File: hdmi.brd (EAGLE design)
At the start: 160 x 100 mm, 130 parts, among them U0 6SLX45CSG324, U1 MT41J64M16, U2 TPD12S016RKTR, U3 TPD12S016RKTR, U4 TPD12S016RKTR, U5 MNR18, U6 MNR18

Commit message: +prj-hdmi.lbr, +5V protection
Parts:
- removed R43: 4.7k, resistor:R0402
- removed U$12: PJ-037A, con-cui:PJ-037A
- removed U$13: FERRITE0603, inductors:0603
- added C15: 0.47n, rcl:C0402
- added R46: 1k, resistor:R0402
- added U$15: PJ-037A, prj-hdmi:PJ-037A
- added U$16: FERRITE0603, inductors:0603
- added U$17: TPS2592BA, prj-hdmi:DRC-S-PVSON-N10
- CONN0, CONN1, CONN2: device con-fci:HDMI_TYPE_A_RECEPTICAL -> prj-hdmi:HDMI_TYPE_A_RECEPTICAL
- CONN3: device con-usb-3:USB-MB-S -> prj-hdmi:USB-MB-S
- IC1: device ftdichip-3:QFN64 -> prj-hdmi:QFN64
- R42: value 10k -> 100k
- U$1: device Abracon:ABM8G-32X25 -> prj-hdmi:ABM8G-32X25
- U$5: device Microchip_By_element14_Batch_1:SOT95P280X145-6N -> prj-hdmi:SOT95P280X145-6N
- U$6: device Micrel Inc:QFN-26-4X4 -> prj-hdmi:QFN-26-4X4
- U$9: device memory-micron:V-PDFN-8_8X6 -> prj-hdmi:V-PDFN-8_8X6
- U0: device xilinx_devices_V6:CS324 -> prj-hdmi:CS324
- U1: device memory-micron:FBGA96-JT -> prj-hdmi:FBGA96-JT
- U2, U3, U4: device Texas Instruments:UQFN24 -> prj-hdmi:UQFN24
- moved R42 97.8 mm to (-148.6, -733.9)
- moved U0 0.31 mm to (-39.4, 9.20)
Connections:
- net N$49 renamed USB_5V_DISABLE
- removed net USB_5V_ERR: R45.1, U$10.4
- new net N$32: C15.1, U$17.1
- new net N$36: R42.2, U$17.10
- new net USB_5V_ACK#: R45.1, R46.1, U$10.4
- new net USB_5V_OFF: R46.2
- net +3V3: now also R26.1
- net +5V: now also U$17.6, U$17.7, U$17.8; no longer R43.2
- net CENTER: now also U$15.CENTER, U$16.1; no longer U$12.CENTER, U$13.1
- net GND: now also C15.2, U$15.BARREL, U$17.TH, U$17.TH@1, U$17.TH@2; no longer U$12.BARREL
- net N$29: now also U$16.2, U$17.2, U$17.3, U$17.4, U$17.5; no longer R26.1
- net USB_PWRSAVE#: no longer R42.2, R43.1

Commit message: began mergin and cleaning up libraries
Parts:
- removed C7: 100u, rcl:C1206
- removed U$11: FERRITE0603, inductors:0603
- added L6: 1A, prj-hdmi:0603
- added R43: 10k, resistor:R0402
- L1, L2, L3: value CIG22E -> 1u; device inductors:2520 -> prj-hdmi:1008
- L4, L5: value FERRITE0402 -> 1A; device inductors:0402 -> prj-hdmi:0402
- LED1, LED2: device led:CHIP-LED0603 -> prj-hdmi:LED-0603
- R42: value 100k -> 47k
- U$10: value TPD4S014DSQRSON -> TPD4S014SON
- U$16: value FERRITE0603 -> 4A; device inductors:0603 -> prj-hdmi:0603
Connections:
- net +1V5: no longer C7.1
- net +3V3: now also R43.2; no longer LED2.A
- net GND: no longer C7.2
- net N$45: now also L6.1; no longer U$11.1
- net N$48: now also L6.2; no longer U$11.2
- net USB_PWRSAVE#: now also R43.1
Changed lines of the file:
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@@
 <element name="C5" library="rcl" package="C0402" value="4.7u" x="-55.88" y="-52.07"/>
 <element name="C6" library="rcl" package="C0402" value="0.47u" x="-55.88" y="-57.15"/>
-<element name="C7" library="rcl" package="C1206" value="100u" x="-54.61" y="-63.5"/>
 <element name="C8" library="rcl" package="C0402" value="0.47u" x="-55.88" y="-69.85"/>
 <element name="R7" library="resistor" package="R0402" value="120" x="-55.88" y="-74.93"/>
@@
 <element name="C48" library="rcl" package="C0402" value="4.7u" x="-113.03" y="-405.13"/>
 <element name="C49" library="rcl" package="C1206" value="100u" x="-111.76" y="-411.48"/>
-<element name="L1" library="inductors" package="2520" value="CIG22E" x="-118.11" y="-411.48"/>
-<element name="L2" library="inductors" package="2520" value="CIG22E" x="-123.19" y="-411.48"/>
-<element name="L3" library="inductors" package="2520" value="CIG22E" x="-128.27" y="-411.48"/>
+<element name="L1" library="prj-hdmi" package="1008" value="1u" x="-118.11" y="-411.48"/>
+<element name="L2" library="prj-hdmi" package="1008" value="1u" x="-123.19" y="-411.48"/>
+<element name="L3" library="prj-hdmi" package="1008" value="1u" x="-128.27" y="-411.48"/>
 <element name="R15" library="resistor" package="R0402" value="309k" x="-128.27" y="-417.83"/>
 <element name="R16" library="resistor" package="R0402" value="71.5k" x="-128.27" y="-422.91"/>
@@
 <element name="R25" library="resistor" package="R0402" value="10k" x="-128.27" y="-483.87"/>
 <element name="R26" library="resistor" package="R0402" value="10k" x="-128.27" y="-488.95"/>
-<element name="L4" library="inductors" package="0402" value="FERRITE0402" x="-128.27" y="-494.03"/>
-<element name="L5" library="inductors" package="0402" value="FERRITE0402" x="-128.27" y="-499.11"/>
+<element name="L4" library="prj-hdmi" package="0402" value="1A" x="-128.27" y="-494.03"/>
+<element name="L5" library="prj-hdmi" package="0402" value="1A" x="-128.27" y="-499.11"/>
 <element name="C53" library="resistor" package="C0402" value="0.1u" x="-128.27" y="-504.19"/>
 <element name="C54" library="resistor" package="C0402" value="4.7u" x="-128.27" y="-509.27"/>
@@
 <element name="R32" library="resistor" package="R0402" value="1k" x="-128.27" y="-574.04"/>
 <element name="R33" library="resistor" package="R0402" value="1k" x="-128.27" y="-579.12"/>
-<element name="LED1" library="led" package="CHIP-LED0603" value="Yellow" x="-133.35" y="-580.39"/>
+<element name="LED1" library="prj-hdmi" package="LED-0603" value="Yellow" x="-133.35" y="-580.39"/>
 <element name="R34" library="resistor" package="R0402" value="4.7k" x="-133.35" y="-584.2"/>
 <element name="R35" library="resistor" package="R0402" value="10k" x="-133.35" y="-589.28"/>
@@
 <element name="R40" library="resistor" package="R0402" value="100" x="-143.51" y="-619.76"/>
 <element name="R41" library="resistor" package="R0402" value="1k" x="-143.51" y="-631.19"/>
-<element name="LED2" library="led" package="CHIP-LED0603" value="Green" x="-142.24" y="-627.38"/>
-<element name="U$11" library="inductors" package="0603" value="FERRITE0603" x="-143.51" y="-650.24"/>
-<element name="U$10" library="Texas Instruments" package="SON10" value="TPD4S014DSQRSON" x="-148.59" y="-654.05"/>
+<element name="LED2" library="prj-hdmi" package="LED-0603" value="Green" x="-142.24" y="-627.38"/>
+<element name="L6" library="prj-hdmi" package="0603" value="1A" x="-143.51" y="-650.24"/>
+<element name="U$10" library="Texas Instruments" package="SON10" value="TPD4S014SON" x="-148.59" y="-654.05"/>
 <element name="R44" library="resistor" package="R0402" value="10k" x="-148.59" y="-660.4"/>
 <element name="R45" library="resistor" package="R0402" value="10k" x="-148.59" y="-680.72"/>
 <element name="R46" library="resistor" package="R0402" value="1k" x="-148.59" y="-690.6768"/>
 <element name="U$15" library="prj-hdmi" package="PJ-037A" value="PJ-037A" x="-141.8844" y="-707.5424"/>
-<element name="U$16" library="inductors" package="0603" value="FERRITE0603" x="-148.59" y="-724.3064"/>
+<element name="U$16" library="prj-hdmi" package="0603" value="4A" x="-148.59" y="-724.3064"/>
 <element name="U$17" library="prj-hdmi" package="DRC-S-PVSON-N10" value="TPS2592BA" x="-147.066" y="-717.9564"/>
 <element name="C15" library="rcl" package="C0402" value="0.47n" x="-148.59" y="-729.0562"/>
-<element name="R42" library="resistor" package="R0402" value="100k" x="-148.59" y="-733.933"/>
+<element name="R42" library="resistor" package="R0402" value="47k" x="-148.59" y="-733.933"/>
+<element name="R43" library="resistor" package="R0402" value="10k" x="-148.59" y="-738.9368"/>
 </elements>
 <signals>
@@
 <contactref element="C6" pad="2"/>
 <contactref element="C5" pad="2"/>
-<contactref element="C7" pad="2"/>
 <contactref element="C13" pad="2"/>
 <contactref element="C16" pad="2"/>
@@
 <wire x1="-55.23" y1="-74.93" x2="-55.23" y2="-80.01" width="0" layer="19" extent="1-1"/>
 <wire x1="-55.23" y1="-69.85" x2="-55.23" y2="-74.93" width="0" layer="19" extent="1-1"/>
-<wire x1="-53.21" y1="-63.5" x2="-55.23" y2="-69.85" width="0" layer="19" extent="1-1"/>
-<wire x1="-55.23" y1="-57.15" x2="-53.21" y2="-63.5" width="0" layer="19" extent="1-1"/>
+<wire x1="-55.23" y1="-57.15" x2="-55.23" y2="-69.85" width="0" layer="19" extent="1-1"/>
 <wire x1="-55.23" y1="-52.07" x2="-55.23" y2="-57.15" width="0" layer="19" extent="1-1"/>
 <wire x1="-56.53" y1="-41.91" x2="-55.23" y2="-52.07" width="0" layer="19" extent="1-1"/>
@@
 <contactref element="R38" pad="2"/>
 <contactref element="R39" pad="2"/>
-<contactref element="LED2" pad="A"/>
 <contactref element="R45" pad="2"/>
 <contactref element="R26" pad="1"/>
+<contactref element="R43" pad="2"/>
 <wire x1="-142.86" y1="-609.6" x2="-142.86" y2="-614.68" width="0" layer="19" extent="1-1"/>
 <wire x1="-142.86" y1="-604.52" x2="-142.86" y2="-609.6" width="0" layer="19" extent="1-1"/>
@@
 <wire x1="-132.7" y1="-584.2" x2="-136.92" y2="-589.91" width="0" layer="19" extent="1-1"/>
 <wire x1="-133.35" y1="-581.14" x2="-132.7" y2="-584.2" width="0" layer="19" extent="1-1"/>
-<wire x1="-142.24" y1="-628.13" x2="-142.86" y2="-614.68" width="0" layer="19" extent="1-1"/>
 <wire x1="-127.62" y1="-553.72" x2="-133.35" y2="-581.14" width="0" layer="19" extent="1-1"/>
 <wire x1="-128.92" y1="-534.67" x2="-127.62" y2="-553.72" width="0" layer="19" extent="1-1"/>
@@
 <wire x1="-89.55" y1="-227.33" x2="-90.245" y2="-266.68" width="0" layer="19" extent="1-1"/>
 <wire x1="-90.245" y1="-205.72" x2="-89.55" y2="-227.33" width="0" layer="19" extent="1-1"/>
-<wire x1="-147.94" y1="-680.72" x2="-142.24" y2="-628.13" width="0" layer="19" extent="1-1"/>
+<wire x1="-147.94" y1="-680.72" x2="-142.86" y2="-614.68" width="0" layer="19" extent="1-1"/>
+<wire x1="-147.94" y1="-738.9368" x2="-147.94" y2="-680.72" width="0" layer="19" extent="1-1"/>
 <wire x1="-43" y1="5.6" x2="-90.245" y2="-205.72" width="0" layer="19" extent="1-1"/>
 <wire x1="-41.4" y1="8.8" x2="-43" y2="5.6" width="0" layer="19" extent="1-1"/>
@@
 <contactref element="C1" pad="1"/>
 <contactref element="C8" pad="1"/>
-<contactref element="C7" pad="1"/>
 <contactref element="C5" pad="1"/>
 <contactref element="C6" pad="1"/>
@@
 <wire x1="-56.53" y1="-80.01" x2="-56.53" y2="-85.09" width="0" layer="19" extent="1-1"/>
 <wire x1="-56.53" y1="-69.85" x2="-56.53" y2="-80.01" width="0" layer="19" extent="1-1"/>
-<wire x1="-56.01" y1="-63.5" x2="-56.53" y2="-69.85" width="0" layer="19" extent="1-1"/>
-<wire x1="-56.53" y1="-57.15" x2="-56.01" y2="-63.5" width="0" layer="19" extent="1-1"/>
+<wire x1="-56.53" y1="-57.15" x2="-56.53" y2="-69.85" width="0" layer="19" extent="1-1"/>
 <wire x1="-56.53" y1="-52.07" x2="-56.53" y2="-57.15" width="0" layer="19" extent="1-1"/>
 <wire x1="-56.53" y1="-22.86" x2="-56.53" y2="-52.07" width="0" layer="19" extent="1-1"/>
@@
 <signal name="USB_PWRSAVE#">
 <contactref element="IC1" pad="59"/>
+<contactref element="R43" pad="1"/>
+<wire x1="-149.24" y1="-738.9368" x2="-83.8" y2="-321.99" width="0" layer="19" extent="1-1"/>
 </signal>
 <signal name="N$45" class="1">
 <contactref element="CONN3" pad="VBUS"/>
-<contactref element="U$11" pad="1"/>
+<contactref element="L6" pad="1"/>
 <wire x1="-144.36" y1="-650.24" x2="-95.29" y2="-328.6" width="0" layer="19" extent="1-1"/>
 </signal>
@@
 </signal>
 <signal name="N$48">
-<contactref element="U$11" pad="2"/>
+<contactref element="L6" pad="2"/>
 <contactref element="U$10" pad="9"/>
 <contactref element="U$10" pad="10"/>

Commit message: +5V supply zener diode and minor misc. changes
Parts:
- removed C49: 100u, rcl:C1206
- added C19: 0.1u, prj-hdmi:0603
- added C7: 100u, prj-hdmi:0603
- added R47: 50, resistor:R0402
- added R48: 100, resistor:R0402
- added U$11: 20V, prj-hdmi:SOD123FL
- L1, L2, L3: value 1u -> 1u, 2.3A
- U$16: value 4A -> 3A
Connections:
- net +3V3: now also R27.2; no longer LED1.A
- net +5V: now also R41.2; no longer C49.1
- net CENTER: now also U$11.C
- net GND: now also C19.2, C7.2, LED2.C, R48.1, U$11.A, U$6.11, U$6.24, U$6.SGND; no longer C49.2, R41.1
- net N$29: now also C19.1, R47.2; no longer U$17.2
- net N$30: now also R47.1, R48.2, U$17.2; no longer U$6.11, U$6.24, U$6.SGND
- net N$33: now also LED1.C; no longer R27.1
- net N$38: now also LED1.A, R27.1; no longer LED1.C, R27.2
- net N$47: now also LED2.A, R41.1; no longer LED2.C, R41.2
- net N$48: now also C7.1

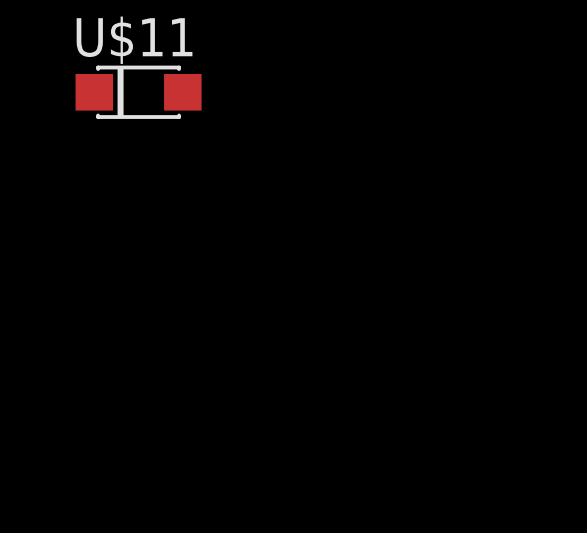
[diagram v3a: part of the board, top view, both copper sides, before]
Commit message: +N-MOSFET at 5V supply, HDMI connector pin swap, minor wiring changes
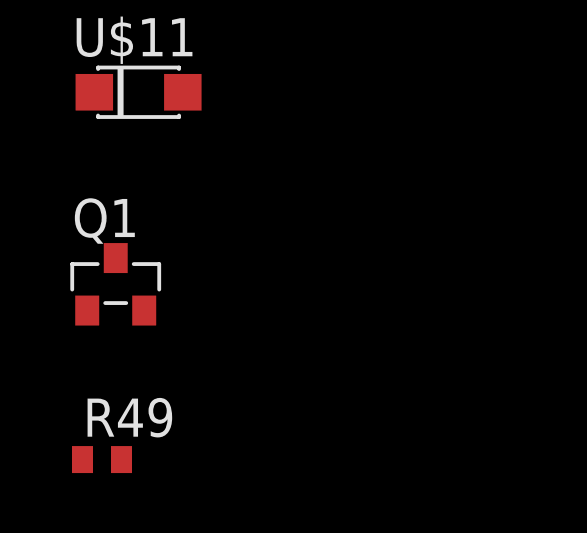
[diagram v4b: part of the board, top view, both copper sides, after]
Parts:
- added Q1: N-MOSFETSOT23, prj-hdmi:SOT23
- added R49: 1k, resistor:R0402
- CONN3: value (none) -> USBMB-S
- IC1: value (none) -> FT2232HQ
- R47: value 50 -> 1k
- R48: value 100 -> 4.7k
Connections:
- removed net 3V3: C13.1, C14.1, C16.1, C17.1, C18.1, C20.1, C21.1, C22.1, C24.1, R29.2, U0.B10, U0.B15, U0.B5, U0.D13, U0.D7, U0.E10, U0.E17, U0.G15, U0.J14, U0.J17, U0.M15, U0.P9, U0.R12, U0.R17, U0.R6, U0.T15, U0.U14, U0.U4, U0.U9
- removed net 3V4: C25.1, C26.1, C27.1, C28.1, C33.1
- removed net 3V5: C29.1, C30.1, C31.1, C32.1
- removed net N$19: C52.2, R20.2
- removed net N$2: IC1.3, U$1.1
- removed net N$4: C44.2, U$1.4
- new net N$49: Q1.1, U$17.9
- new net OUT@8: Q1.2, R49.2, U$17.6, U$17.7, U$17.8
- net +1V2: now also C29.1, C30.1, C31.1, C32.1
- net +3V3: now also C13.1, C14.1, C16.1, C17.1, C18.1, C20.1, C21.1, C22.1, C24.1, C25.1, C26.1, C27.1, C28.1, C33.1, C57.2, R29.2, U0.B10, U0.B15, U0.B5, U0.D13, U0.D7, U0.E10, U0.E17, U0.G15, U0.J14, U0.J17, U0.M15, U0.P9, U0.R12, U0.R17, U0.R6, U0.T15, U0.U14, U0.U4, U0.U9; no longer C57.1
- net +5V: now also Q1.3; no longer U$17.6, U$17.7, U$17.8
- net DDR3_A12: now also U0.G6
- net DDR3_DQ3: now also U1.F8
- net DDR3_DQ4: no longer U1.F8
- net GND: now also C43.2, C44.2, C52.2, C57.1, R20.2, U$1.2, U$1.4; no longer C43.1, C44.1, C57.2
- net HDMI_RX0_CEC: now also U2.6; no longer U2.24
- net HDMI_RX0_CEC_3V3: now also U2.24; no longer U2.6
- net HDMI_RX0_SCL_3V3: now also U2.1; no longer U2.7
- net HDMI_RX0_SCL_5V: now also U2.7; no longer U2.1
- net HDMI_RX0_SDA_3V3: now also U2.2; no longer U2.8
- net HDMI_RX0_SDA_5V: now also U2.8; no longer U2.2
- net HDMI_RX1_CEC: now also U3.6; no longer U3.24
- net HDMI_RX1_CEC_3V3: now also U3.24; no longer U3.6
- net HDMI_RX1_SCL_3V3: now also U3.1; no longer U3.7
- net HDMI_RX1_SCL_5V: now also U3.7; no longer U3.1
- net HDMI_RX1_SDA_3V3: now also U3.2; no longer U3.8
- net HDMI_RX1_SDA_5V: now also U3.8; no longer U3.2
- net HDMI_TX0_CEC: now also U4.6; no longer U4.24
- net HDMI_TX0_CEC_3V3: now also U4.24; no longer U4.6
- net HDMI_TX0_HPD_3V3: now also U4.3; no longer U4.9
- net HDMI_TX0_HPD_5V: now also U4.9; no longer U4.3
- net HDMI_TX0_SCL_3V3: now also U4.1; no longer U4.7
- net HDMI_TX0_SCL_5V: now also U4.7; no longer U4.1
- net HDMI_TX0_SDA_3V3: now also U4.2; no longer U4.8
- net HDMI_TX0_SDA_5V: now also U4.8; no longer U4.2
- net N$1: now also C44.1
- net N$10: now also U$5.3
- net N$5: now also C43.1, IC1.3, U$1.1; no longer C43.2, U$1.2
- net USB_5V_DISABLE: now also R49.1

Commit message: +Oscillator
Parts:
- added C23: 0.1u, rcl:C0402
- added U7: 20Mhz, prj-hdmi:CRYSTAL-OSC-SMD-2.5X2
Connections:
- new net FPGA_OSC: U0.T10, U7.3
- net +3V3: now also C23.1, U7.1, U7.4
- net GND: now also C23.2, U7.2
- net HDMI_TX0_CEC_3V3: now also U0.N8; no longer U0.T10
- net HDMI_TX0_HPD_3V3: now also U0.M8; no longer U0.R10
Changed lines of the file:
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@@
 <element name="Q1" library="prj-hdmi" package="SOT23" value="N-MOSFETSOT23" x="-148.1328" y="-773.4554"/>
 <element name="R49" library="resistor" package="R0402" value="1k" x="-148.59" y="-779.272"/>
+<element name="U7" library="prj-hdmi" package="CRYSTAL-OSC-SMD-2.5X2" value="20Mhz" x="-151.9174" y="-778.764"/>
+<element name="C23" library="rcl" package="C0402" value="0.1u" x="-153.4668" y="-784.1488"/>
 </elements>
 <signals>
@@
 <contactref element="U$1" pad="4"/>
 <contactref element="C57" pad="1"/>
+<contactref element="C43" pad="2"/>
+<contactref element="C44" pad="2"/>
 <contactref element="U$1" pad="2"/>
-<contactref element="C44" pad="2"/>
-<contactref element="C43" pad="2"/>
+<contactref element="U7" pad="2"/>
+<contactref element="C23" pad="2"/>
 <wire x1="-88.25" y1="-161.29" x2="-88.25" y2="-166.37" width="0" layer="19" extent="1-1"/>
 <wire x1="-88.25" y1="-171.45" x2="-88.25" y2="-166.37" width="0" layer="19" extent="1-1"/>
@@
 <wire x1="-149.24" y1="-761.5936" x2="-147.74" y2="-753.5672" width="0" layer="19" extent="1-1"/>
 <wire x1="-145.8958" y1="-767.0292" x2="-149.24" y2="-761.5936" width="0" layer="19" extent="1-1"/>
+<wire x1="-151.0174" y1="-779.464" x2="-145.8958" y2="-767.0292" width="0" layer="19" extent="1-1"/>
+<wire x1="-152.8168" y1="-784.1488" x2="-151.0174" y2="-779.464" width="0" layer="19" extent="1-1"/>
 </signal>
 <signal name="+3V3" class="1">
@@
 <contactref element="C33" pad="1"/>
 <contactref element="C57" pad="2"/>
+<contactref element="U7" pad="1"/>
+<contactref element="U7" pad="4"/>
+<contactref element="C23" pad="1"/>
 <wire x1="-142.86" y1="-609.6" x2="-142.86" y2="-614.68" width="0" layer="19" extent="1-1"/>
 <wire x1="-142.86" y1="-604.52" x2="-142.86" y2="-609.6" width="0" layer="19" extent="1-1"/>
@@
 <wire x1="-147.94" y1="-680.72" x2="-142.86" y2="-614.68" width="0" layer="19" extent="1-1"/>
 <wire x1="-147.94" y1="-738.9368" x2="-147.94" y2="-680.72" width="0" layer="19" extent="1-1"/>
+<wire x1="-152.8174" y1="-778.064" x2="-147.94" y2="-738.9368" width="0" layer="19" extent="1-1"/>
+<wire x1="-152.8174" y1="-779.464" x2="-152.8174" y2="-778.064" width="0" layer="19" extent="1-1"/>
+<wire x1="-154.1168" y1="-784.1488" x2="-152.8174" y2="-779.464" width="0" layer="19" extent="1-1"/>
 <wire x1="-43.8" y1="3.2" x2="-56.53" y2="-107.95" width="0" layer="19" extent="1-1"/>
 <wire x1="-42.2" y1="4.8" x2="-43.8" y2="3.2" width="0" layer="19" extent="1-1"/>
@@
 <signal name="HDMI_TX0_HPD_3V3">
 <contactref element="U4" pad="3"/>
-<contactref element="U0" pad="R10"/>
-<wire x1="-39" y1="4.8" x2="-89.27" y2="-303.415" width="0" layer="19" extent="1-1"/>
+<contactref element="U0" pad="M8"/>
+<wire x1="-40.6" y1="7.2" x2="-89.27" y2="-303.415" width="0" layer="19" extent="1-1"/>
 </signal>
 <signal name="HDMI_TX0_CEC_3V3">
 <contactref element="U4" pad="24"/>
-<contactref element="U0" pad="T10"/>
-<wire x1="-39" y1="4" x2="-90.245" y2="-302.64" width="0" layer="19" extent="1-1"/>
+<contactref element="U0" pad="N8"/>
+<wire x1="-40.6" y1="6.4" x2="-90.245" y2="-302.64" width="0" layer="19" extent="1-1"/>
 </signal>
 <signal name="HDMI_TX0_SCL_3V3">
@@
 <wire x1="-86.95" y1="-323.64" x2="-109.05" y2="-333.54" width="0" layer="19" extent="1-1"/>
 </signal>
+<signal name="FPGA_OSC">
+<contactref element="U0" pad="T10"/>
+<contactref element="U7" pad="3"/>
+<wire x1="-39" y1="4" x2="-151.0174" y2="-778.064" width="0" layer="19" extent="1-1"/>
+</signal>
 </signals>

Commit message: +IO
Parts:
- removed C23: 0.1u, rcl:C0402
- removed U7: 20Mhz, prj-hdmi:CRYSTAL-OSC-SMD-2.5X2
- added C49: 0.1u, rcl:C0402
- added SV1: JTAG, prj-hdmi:MA06-1
- added SV2: FE10-2, prj-hdmi:FE10-2
- added U$12: SN74LVC8T245RHLR, prj-hdmi:RHL_R-PVQFN-N24
- added U8: 20Mhz, prj-hdmi:CRYSTAL-OSC-SMD-2.5X2
- L1, L2, L3: value 1u, 2.3A -> 1u, 3A
- R44: value 10k -> 4.7k
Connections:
- removed net FPGA_OSC: U0.T10, U7.3
- removed net USB_PWREN#: IC1.60
- new net FPGA_OSC1: U0.A9, U8.3
- new net IO_0: SV2.5, U0.B11
- new net IO_1: SV2.7, U0.A11
- new net IO_10: U$12.5, U0.C15
- new net IO_10_5V: SV2.10, U$12.19
- new net IO_11: U$12.6, U0.A15
- new net IO_11_5V: SV2.12, U$12.18
- new net IO_12: U$12.7, U0.D14
- new net IO_12_5V: SV2.14, U$12.17
- new net IO_13: U$12.8, U0.C14
- new net IO_13_5V: SV2.16, U$12.16
- new net IO_14: U$12.9, U0.B16
- new net IO_14_5V: SV2.18, U$12.15
- new net IO_15: U$12.10, U0.A16
- new net IO_15_5V: SV2.20, U$12.14
- new net IO_2: SV2.9, U0.B12
- new net IO_3: SV2.11, U0.A12
- new net IO_4: SV2.13, U0.C13
- new net IO_5: SV2.15, U0.A13
- new net IO_6: SV2.17, U0.B14
- new net IO_7: SV2.19, U0.A14
- new net IO_8: U$12.3, U0.F13
- new net IO_8-15_DIR: U$12.2, U0.F9
- new net IO_8-15_DISABLE: U$12.22, U0.G9
- new net IO_8_5V: SV2.6, U$12.21
- new net IO_9: U$12.4, U0.E13
- new net IO_9_5V: SV2.8, U$12.20
- net +3V3: now also C49.1, SV1.1, SV2.1, U$12.1, U8.1, U8.4; no longer C23.1, U7.1, U7.4
- net +5V: now also SV2.2, U$12.23, U$12.24
- net GND: now also C49.2, SV1.2, SV2.3, SV2.4, U$12.11, U$12.12, U$12.13, U$12.ETP, U$12.ETP@1, U$12.ETP@2, U$12.ETP@3, U8.2; no longer C23.2, U7.2
- net USB_5V_OFF: now also U0.H13
- net USB_SUSPEND#: now also U0.H14
- net USB_TCK: now also SV1.3
- net USB_TDI: now also SV1.5
- net USB_TDO: now also SV1.4
- net USB_TMS: now also SV1.6
